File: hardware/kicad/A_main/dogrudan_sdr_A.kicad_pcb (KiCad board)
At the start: 6 copper layers, 235 x 225 mm, 297 parts, among them J1 XT60, J10 JTAG 2x3, J20 SMA A1, J21 SMA B1, J22 SMA A2, J23 SMA B2, J30 SMA TX1, J31 SMA TX2, J32 SMA TX3, J33 SMA TX4, J40 HR911130A, J41 HR911130A, J60 GPS modul, J61 SMA 10MHz ref, J62 DAC modul, J63 C kartina, J64 UART 3.3V, J65 C kartina #2, J66 D kartina, Q1 DMP3098L, SW1 PROG, T1 ADT1-1WT+, T10 ADT1-1WT+, T11 ADT1-1WT+, T12 ADT1-1WT+, T13 ADT1-1WT+, T2 ADT1-1WT+, T3 ADT1-1WT+, T4 ADT1-1WT+, U1 TPS62130, U10 LFE5U-25F-7BG256I, U11 W25Q128JVSIQ, U15 ADCLK846BCPZ, U16 SN65LVDS2DBVR, U17 SN65LVDS2DBVR, U18 SN65LVDS2DBVR, U2 TPS62130, U20 AD9251BCPZ-80, U21 AD9251BCPZ-80, U3 TPS7A2033, U30 AD9767ASTZ, U31 AD9767ASTZ, U4 ADP150, U40 RTL8211FI-CG, U41 RTL8211FI-CG, U5 ADP150, U50 W9825G6KH-6I, U6 ADP150, U62 TLV3501AIDBVR, U7 ADP150, U8 ADP150, U9 ADP150, Y10 ABLNO-V-80.000MHZ, Y610 25MHz CL12pF, Y626 25MHz CL12pF

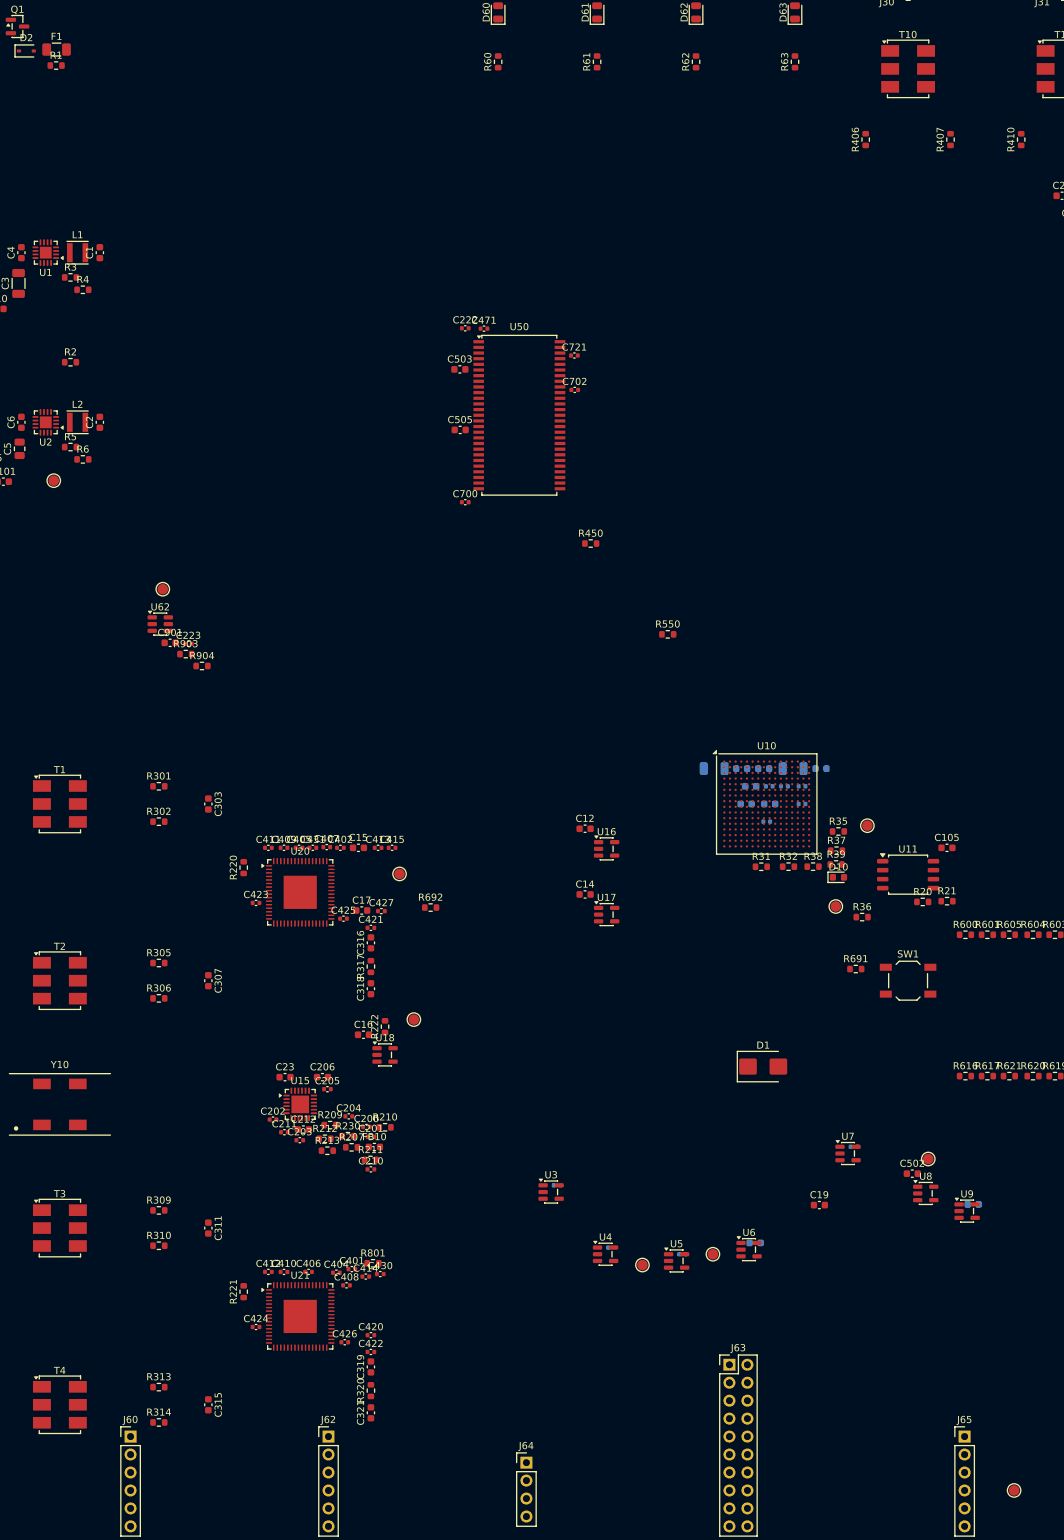
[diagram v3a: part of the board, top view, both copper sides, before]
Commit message: Give each regulator the part number its rail needs
A fixed-output LDO carries its voltage in the part number. If the
number is wrong the schematic does not change: the netlist is correct,
ERC is clean, DRC is clean, and the rail comes up at the wrong
voltage.

U3 was specified as TPS7A2033. The last two digits are the output, so
33 is 3.3 V and 18 is 1.8 V. Its output feeds +1V8, which supplies the
FPGA's bank 6 and 3 VCCIO across twenty pads. The wiring was correct
and only the part number was wrong.

The six ADP150 regulators all carried the value "ADP150" and collapsed
into one BOM line under one code, which is the 2.5 V version. Their
outputs are 1.8, 1.8, 1.8, 2.5, 3.3 and 3.3 V. That line would have
put 2.5 V on both ADC supplies, and the AD9251 has an absolute maximum
of 2.0 V on AVDD. Each rail now names its own variant and the BOM has
separate lines.

regulator_denetim checks this class. It reads the voltage from the
part number, reads it from the rail name and compares them. It also
requires an LDO to have an input higher than its output by at least
the dropout voltage.
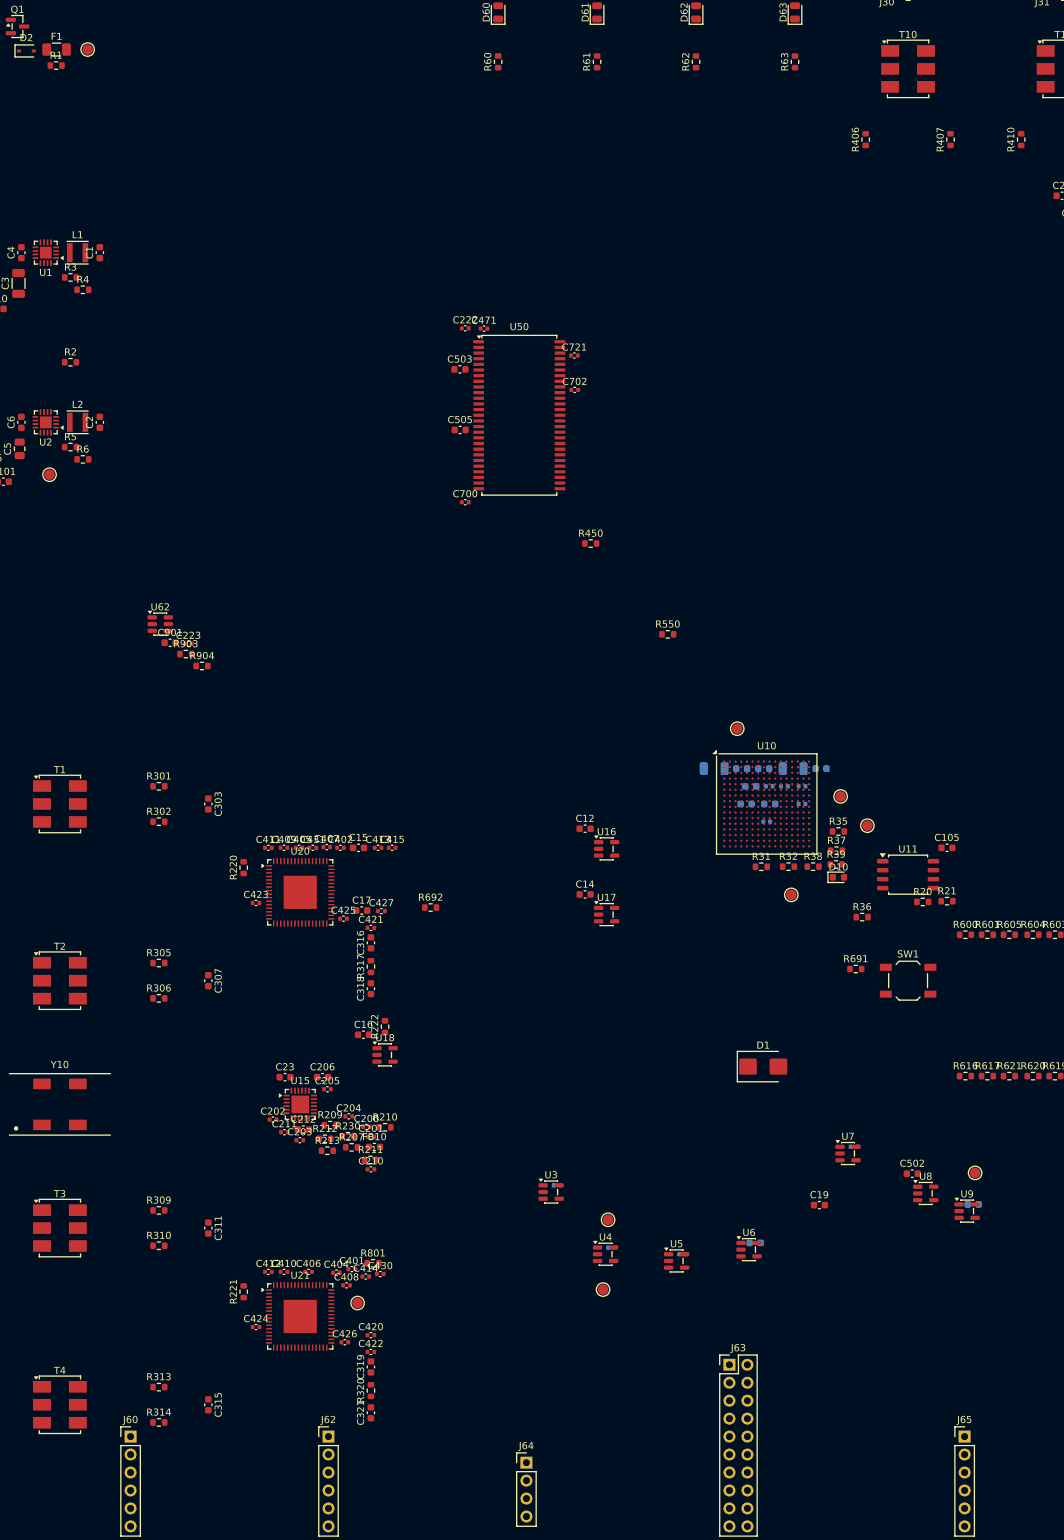
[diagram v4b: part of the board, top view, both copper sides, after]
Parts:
- U3: value TPS7A2033 -> TPS7A2018
- U4, U5, U9: value ADP150 -> ADP150-1.8
- U6, U7: value ADP150 -> ADP150-3.3
- U8: value ADP150 -> ADP150-2.5
- moved TP6 242.4 mm to (33.9, 13.3)
- moved TP10 83.6 mm to (125.8, 109.3)
- moved TP7 68.1 mm to (140.5, 118.9)
- moved TP2 57.1 mm to (107.6, 178.8)
- moved TP3 50.7 mm to (72.1, 190.6)
- moved TP4 6.91 mm to (159.5, 172.2)
- moved TP5 6.56 mm to (106.8, 188.7)
- moved TP8 6.51 mm to (133.5, 132.9)
- moved TP1 1.03 mm to (28.5, 73.4)

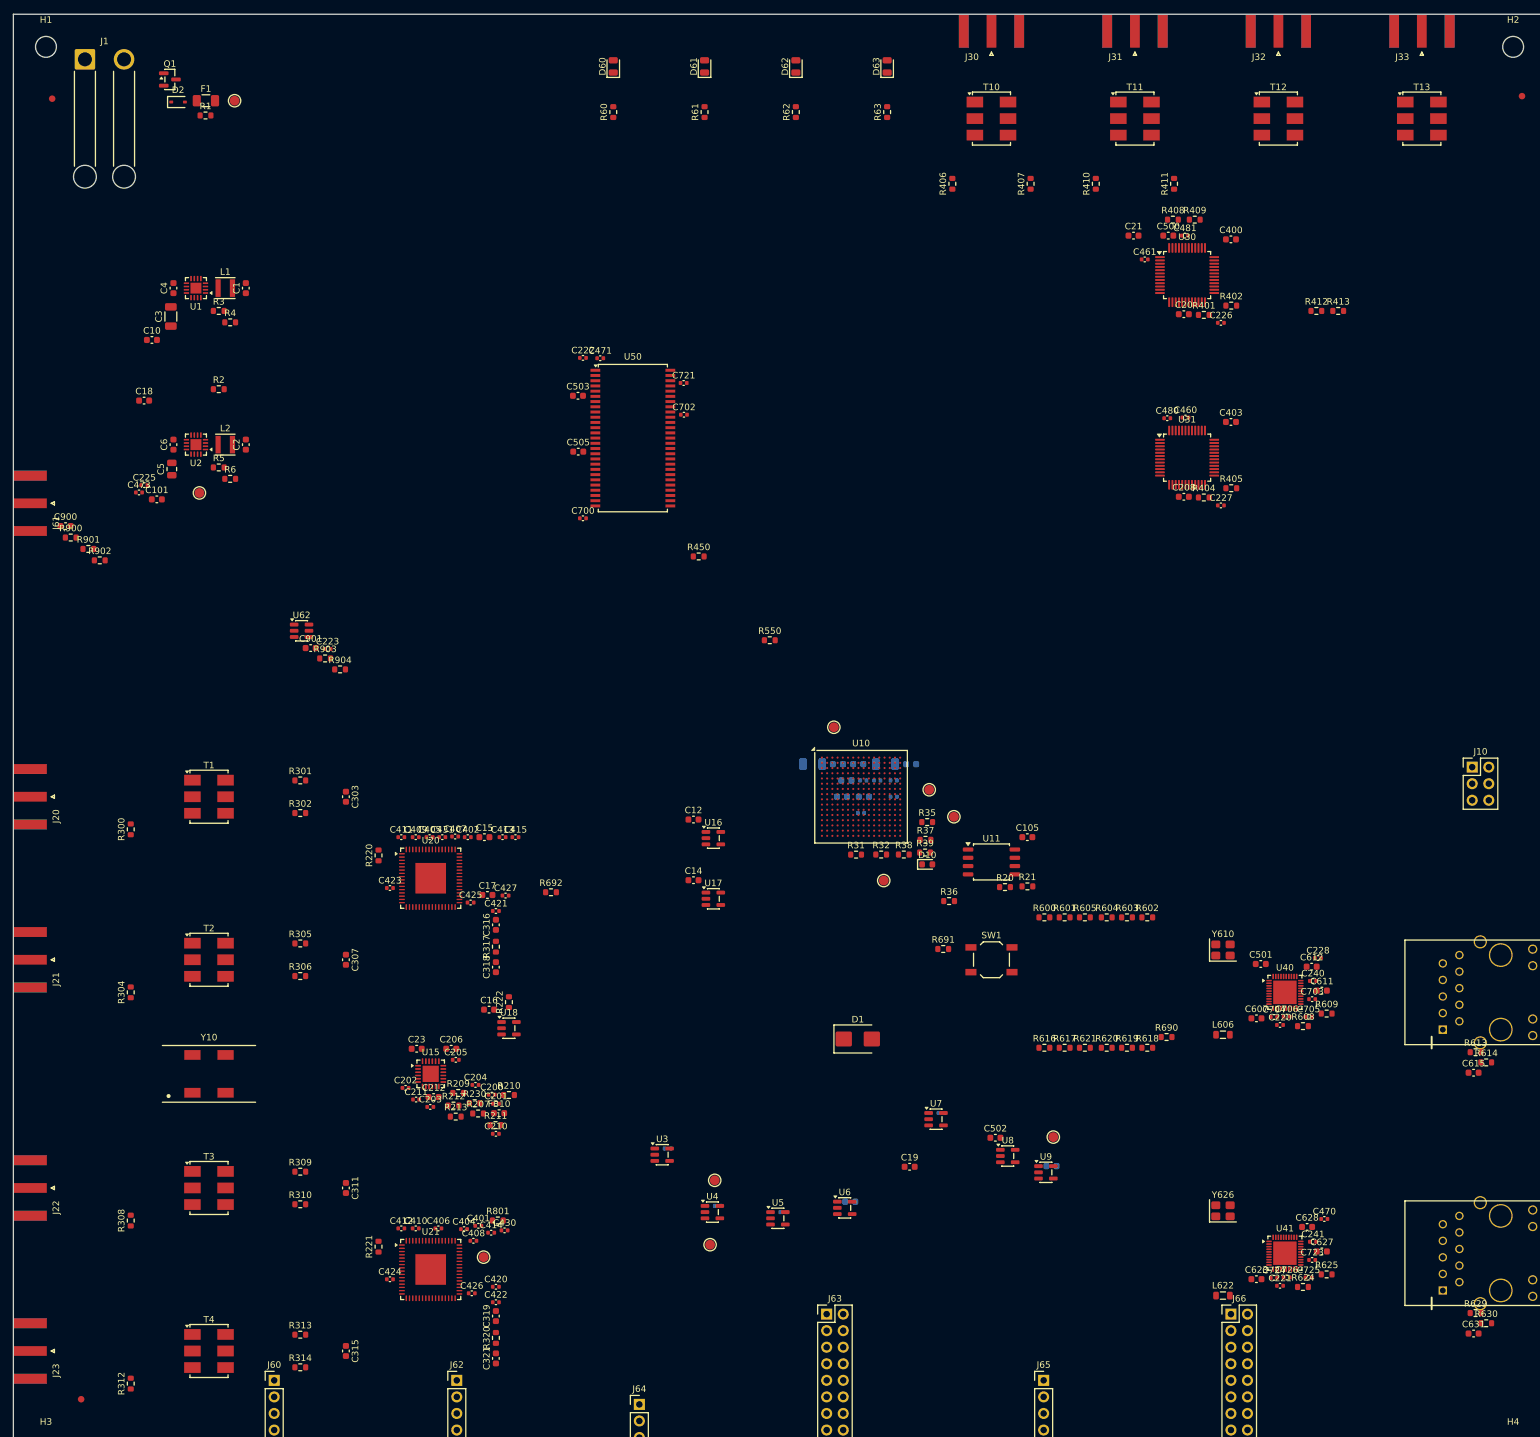
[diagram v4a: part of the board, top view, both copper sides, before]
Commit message: Name the copyright holder and stamp it into the generated files
The repository had three licence files and no statement of who owns
the work. The only record of authorship was the git author field.

Copyleft depends on that statement. GPL and CERN-OHL-S work because
the holder grants permission on condition of reciprocity; with no
holder named there is nobody to require it from a downstream user.
Naming the author keeps the design open rather than closing it.

kicad/telif.py is the single source. The line reaches the schematics
through their title block and not through the generators, because
every schematic file is rewritten on each build and a header placed in
a generator would disappear at the first regeneration. All 23
schematics carry it. 109 source files have SPDX headers, split by the
project's own table: generators and the layout chain are hardware
under CERN-OHL-S-2.0, HDL and the audit tools are software under
GPL-3.0-only.

Board C's inductors also move to footprints that match parts that can
be bought. All of them sat on 0805 pads. Of the values this design
needs, 33 to 220 nH are 0603 parts, 470 and 820 nH are 0805, and
everything from 1000 nH upward is 1210, which is 3.2 by 2.5 mm and
does not fit an 0805 land. 32 inductors could not have been soldered.

A symbol-against-footprint check cannot find this. Those two agreed
with each other; what was wrong was the body size of the real part
behind the footprint.
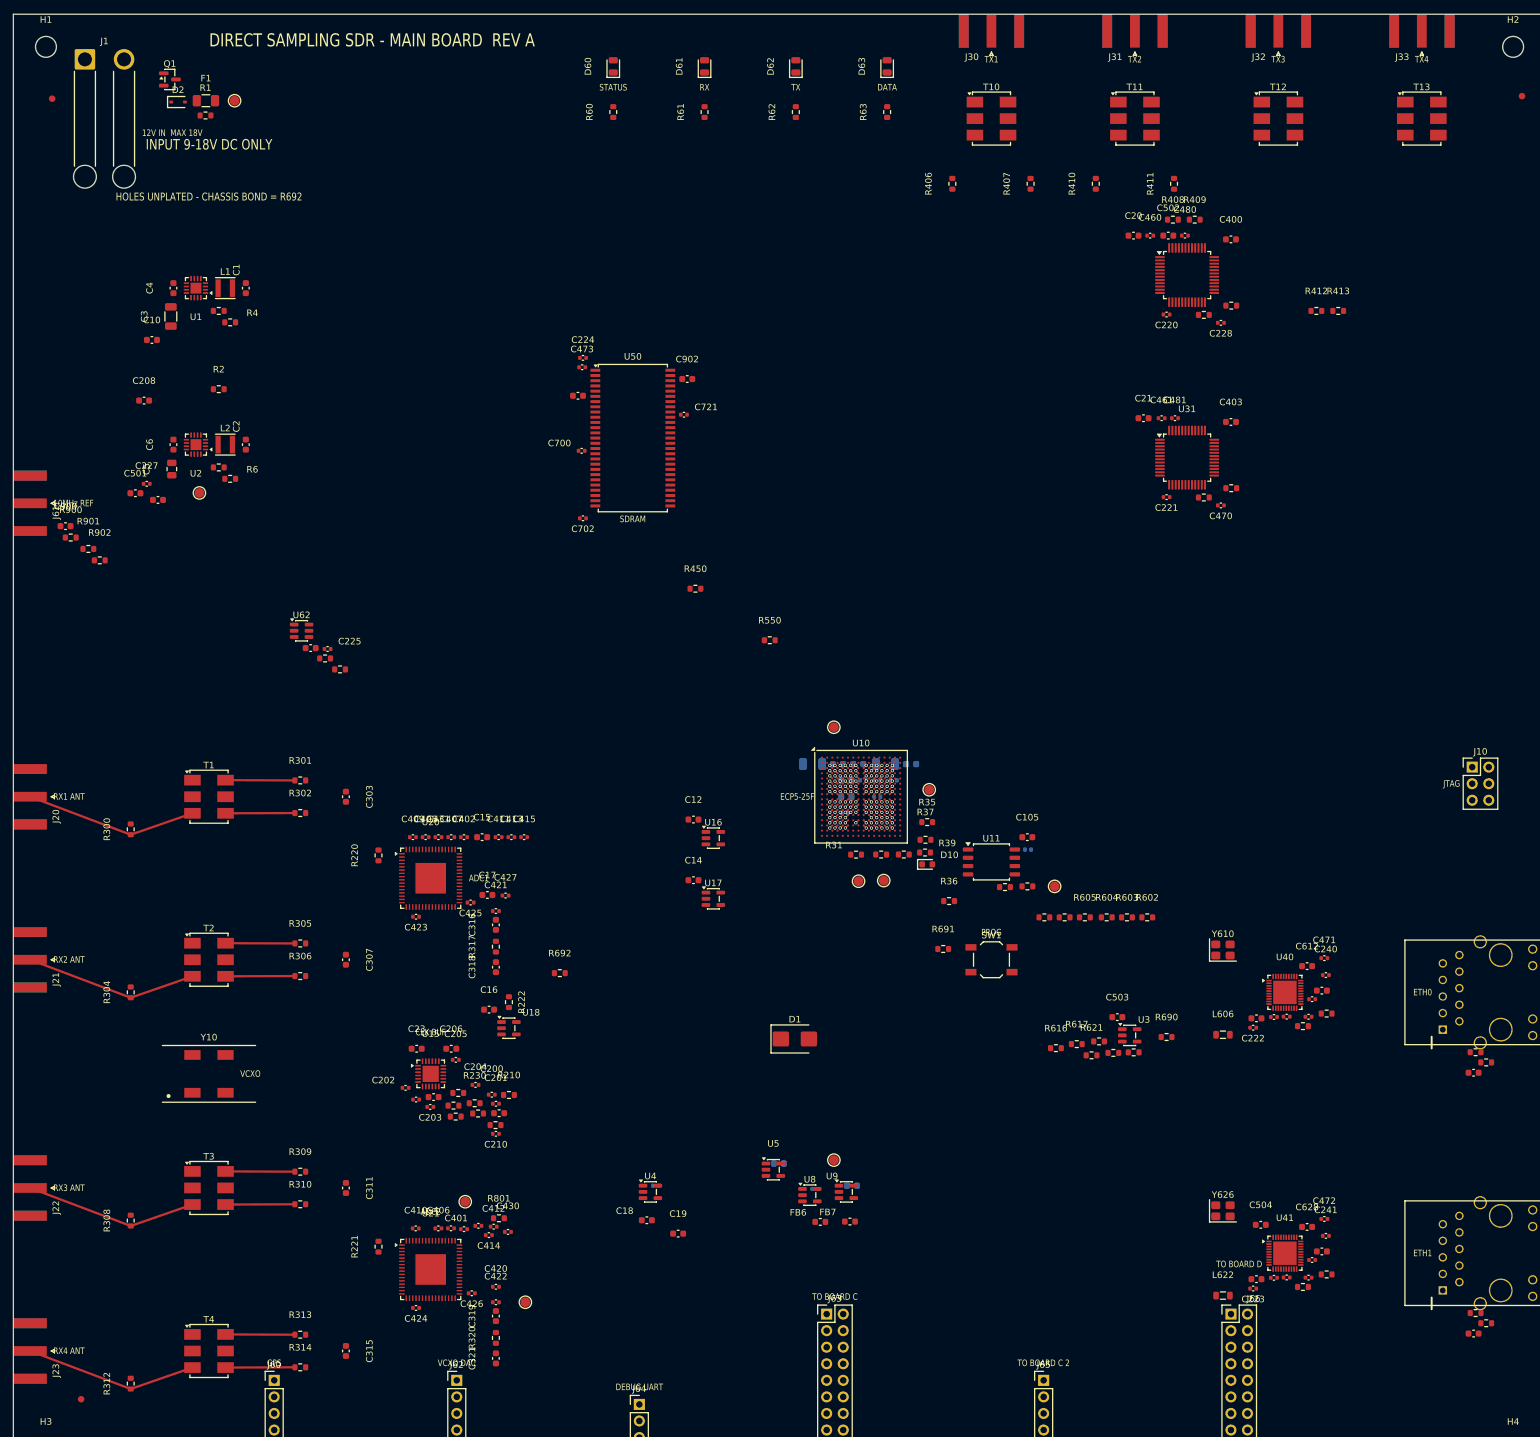
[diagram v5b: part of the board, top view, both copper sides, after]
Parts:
- removed U6, U7: ADP150-3.3, TSOT-23-5
- added FB6: ferrit 600R, L_0603_1608Metric, F.Cu at (123.8, 185.2)
- added FB7: ferrit 600R, L_0603_1608Metric, F.Cu at (128.3, 185.2)
- C18, C20: value 1uF -> 10uF
- C19, C21: value 1uF -> 100nF
- C224, C472, C504, C902: moved to F.Cu
- C226, C500: moved to B.Cu
- moved C501 187.1 mm to (18.7, 73.5)
- moved C223 172.5 mm to (190.1, 195.4)
- moved C227 164.8 mm to (20.5, 72.0)
- moved C208 160.1 mm to (20.1, 59.2)
- moved C500 154.3 mm to (117.4, 176.2)
- moved C18 147.5 mm to (97.2, 184.9)
- moved C222 145.3 mm to (190.1, 155.4)
- moved C471 144.2 mm to (201.0, 144.8)
- moved C502 140.9 mm to (177.1, 34.0)
- moved C902 128.6 mm to (103.3, 55.9)
- moved C503 126.2 mm to (169.3, 153.8)
- moved C221 122.2 mm to (176.8, 74.0)
- moved C470 110.6 mm to (185.2, 75.3)
- moved C220 110.3 mm to (176.8, 46.0)
- moved C228 98.5 mm to (185.2, 47.3)
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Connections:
- C18 pad 1: +3V3 -> +3V3_CLK
- C20 pad 1: +3V3 -> +3V3_A
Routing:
- net RF_A1: track 0.00 -> 26.5 mm
- net RF_B2: track 0.00 -> 26.5 mm
- net RF_B1: track 0.00 -> 26.5 mm
- net RF_A2: track 0.00 -> 26.5 mm
- net SEC_B2_P: track 0.00 -> 10.6 mm
- net SEC_B2_N: track 0.00 -> 10.6 mm
- net SEC_B1_P: track 0.00 -> 10.6 mm
- net SEC_B1_N: track 0.00 -> 10.6 mm
- net SEC_A2_P: track 0.00 -> 10.6 mm
- net SEC_A2_N: track 0.00 -> 10.6 mm
- net SEC_A1_P: track 0.00 -> 10.6 mm
- net SEC_A1_N: track 0.00 -> 10.6 mm
- net GND: track 0.00 -> 8.49 mm, vias 0 -> 15
- net +3V3: track 0.00 -> 5.09 mm, vias 0 -> 9
- net +1V1: track 0.00 -> 3.39 mm, vias 0 -> 6
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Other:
- board text added: "​10MHz REF"
- board text added: "​12V IN MAX 18V"
- board text added: "​ADC1"
- board text added: "​ADC2"
- board text added: "​CLK BUF"
- board text added: "​DATA"
- board text added: "​DEBUG UART"
- board text added: "​DIRECT SAMPLING SDR - MAIN BOARD REV A"
- board text added: "​ECP5-25F"
- board text added: "​ETH0"
- board text added: "​ETH1"
- board text added: "​GPS"
- board text added: "​HOLES UNPLATED - CHASSIS BOND = R692"
- board text added: "​INPUT 9-18V DC ONLY"
- board text added: "​JTAG"
- board text added: "​PROG"
- board text added: "​RX"
- board text added: "​RX1 ANT"
- board text added: "​RX2 ANT"
- board text added: "​RX3 ANT"
- board text added: "​RX4 ANT"
- board text added: "​SDRAM"
- board text added: "​STATUS"
- board text added: "​TO BOARD C"
- board text added: "​TO BOARD C 2"
- board text added: "​TO BOARD D"
- board text added: "​TX"
- board text added: "​TX1"
- board text added: "​TX2"
- board text added: "​TX3"
- board text added: "​TX4"
- board text added: "​VCXO"
- board text added: "​VCXO DAC"
